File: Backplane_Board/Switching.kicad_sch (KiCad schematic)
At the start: 60 parts, among them J37 Conn_01x02, J38 Conn_01x02, J39 Conn_01x02, J40 Conn_01x02, J41 Conn_01x02, J42 Conn_01x02, Q4 ZXMN3A14F, Q5 ZXMN3A14F, Q6 ZXMN3A14F, Q7 ZXMN3A14F, Q8 ZXMN3A14F, Q9 ZXMN3A14F

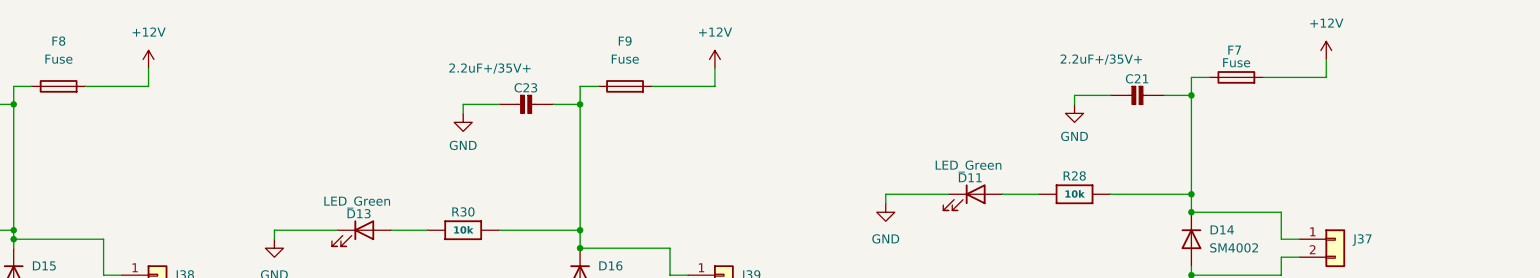
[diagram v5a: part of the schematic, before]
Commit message: got the power input shut layout done ish
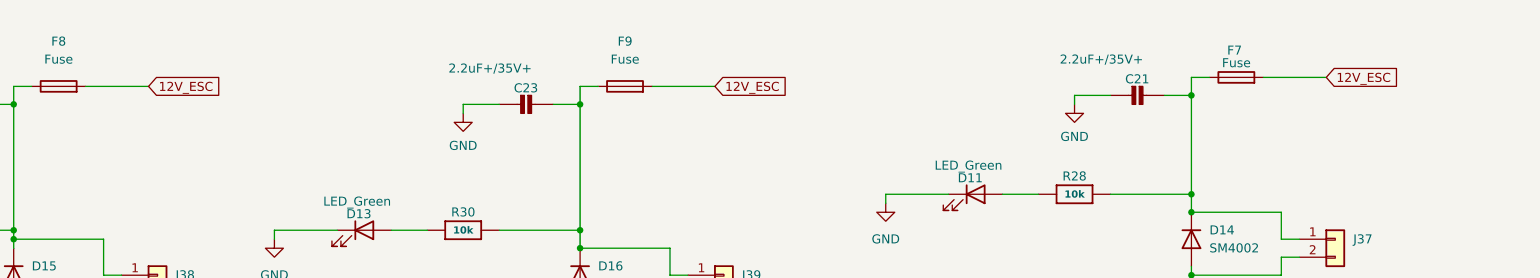
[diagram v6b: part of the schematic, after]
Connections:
- net +12V renamed 12V_ESC
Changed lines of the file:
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@@
 	(wire
 		(pts
-			(xy 162.56 20.32) (xy 162.56 22.86)
-		)
-		(stroke
-			(width 0)
-			(type default)
-		)
-	)
-	(wire
-		(pts
 			(xy 35.56 90.17) (xy 35.56 87.63)
 		)
@@
 	(wire
 		(pts
-			(xy 82.55 20.32) (xy 82.55 22.86)
-		)
-		(stroke
-			(width 0)
-			(type default)
-		)
-	)
-	(wire
-		(pts
 			(xy 143.51 54.61) (xy 156.21 54.61)
 		)
@@
 	(wire
 		(pts
-			(xy 248.92 19.05) (xy 248.92 21.59)
-		)
-		(stroke
-			(width 0)
-			(type default)
-		)
-	)
-	(wire
-		(pts
 			(xy 72.39 140.97) (xy 72.39 144.78)
 		)
@@
 		)
 	)
+	(global_label "12V_ESC"
+		(shape input)
+		(at 248.92 21.59 0)
+		(fields_autoplaced yes)
+		(effects
+			(font
+				(size 1.27 1.27)
+			)
+			(justify left)
+		)
+		(property "Intersheetrefs" "${INTERSHEET_REFS}"
+			(at 260.0089 21.59 0)
+			(effects
+				(font
+					(size 1.27 1.27)
+				)
+				(justify left)
+				(hide yes)
+			)
+		)
+	)
 	(global_label "SW5"
 		(shape input)
@@
 		)
 	)
+	(global_label "12V_ESC"
+		(shape input)
+		(at 162.56 22.86 0)
+		(fields_autoplaced yes)
+		(effects
+			(font
+				(size 1.27 1.27)
+			)
+			(justify left)
+		)
+		(property "Intersheetrefs" "${INTERSHEET_REFS}"
+			(at 173.6489 22.86 0)
+			(effects
+				(font
+					(size 1.27 1.27)
+				)
+				(justify left)
+				(hide yes)
+			)
+		)
+	)
+	(global_label "12V_ESC"
+		(shape input)
+		(at 82.55 22.86 0)
+		(fields_autoplaced yes)
+		(effects
+			(font
+				(size 1.27 1.27)
+			)
+			(justify left)
+		)
+		(property "Intersheetrefs" "${INTERSHEET_REFS}"
+			(at 93.6389 22.86 0)
+			(effects
+				(font
+					(size 1.27 1.27)
+				)
+				(justify left)
+				(hide yes)
+			)
+		)
+	)
 	(global_label "SW0"
 		(shape input)
@@
 	)
 	(symbol
-		(lib_id "power:+12V")
-		(at 82.55 20.32 0)
-		(unit 1)
-		(exclude_from_sim no)
-		(in_bom yes)
-		(on_board yes)
-		(dnp no)
-		(fields_autoplaced yes)
-		(property "Reference" "#PWR083"
-			(at 82.55 24.13 0)
-			(effects
-				(font
-					(size 1.27 1.27)
-				)
-				(hide yes)
-			)
-		)
-		(property "Value" "+12V"
-			(at 82.55 15.24 0)
-			(effects
-				(font
-					(size 1.27 1.27)
-				)
-			)
-		)
-		(property "Footprint" ""
-			(at 82.55 20.32 0)
-			(effects
-				(font
-					(size 1.27 1.27)
-				)
-				(hide yes)
-			)
-		)
-		(property "Datasheet" ""
-			(at 82.55 20.32 0)
-			(effects
-				(font
-					(size 1.27 1.27)
-				)
-				(hide yes)
-			)
-		)
-		(property "Description" "Power symbol creates a global label with name \"+12V\""
-			(at 82.55 20.32 0)
-			(effects
-				(font
-					(size 1.27 1.27)
-				)
-				(hide yes)
-			)
-		)
-		(pin "1"
-		)
-		(instances
-			(project "Backplane_Board"
-				(path "/4484cfee-9e43-4cef-88b4-a8ca308542b4/31bf6b29-9be4-43f9-9eab-c84ca2b3429e"
-					(reference "#PWR083")
-					(unit 1)
-				)
-			)
-		)
-	)
-	(symbol
 		(lib_id "power:GND")
 		(at 143.51 69.85 0)
@@
 	)
 	(symbol
-		(lib_id "power:+12V")
-		(at 248.92 19.05 0)
-		(unit 1)
-		(exclude_from_sim no)
-		(in_bom yes)
-		(on_board yes)
-		(dnp no)
-		(fields_autoplaced yes)
-		(property "Reference" "#PWR082"
-			(at 248.92 22.86 0)
-			(effects
-				(font
-					(size 1.27 1.27)
-				)
-				(hide yes)
-			)
-		)
-		(property "Value" "+12V"
-			(at 248.92 13.97 0)
-			(effects
-				(font
-					(size 1.27 1.27)
-				)
-			)
-		)
-		(property "Footprint" ""
-			(at 248.92 19.05 0)
-			(effects
-				(font
-					(size 1.27 1.27)
-				)
-				(hide yes)
-			)
-		)
-		(property "Datasheet" ""
-			(at 248.92 19.05 0)
-			(effects
-				(font
-					(size 1.27 1.27)
-				)
-				(hide yes)
-			)
-		)
-		(property "Description" "Power symbol creates a global label with name \"+12V\""
-			(at 248.92 19.05 0)
-			(effects
-				(font
-					(size 1.27 1.27)
-				)
-				(hide yes)
-			)
-		)
-		(pin "1"
-		)
-		(instances
-			(project "Backplane_Board"
-				(path "/4484cfee-9e43-4cef-88b4-a8ca308542b4/31bf6b29-9be4-43f9-9eab-c84ca2b3429e"
-					(reference "#PWR082")
-					(unit 1)
-				)
-			)
-		)
-	)
-	(symbol
 		(lib_id "Adafruit MOSFET Driver STEMMA Breakout-eagle-import:CAP_CERAMIC0805-NOOUTLINE")
 		(at 140.97 125.73 270)
@@
 					(unit 1)
 				)
-			)
-		)
-	)
-	(symbol
-		(lib_id "power:+12V")
-		(at 162.56 20.32 0)
-		(unit 1)
-		(exclude_from_sim no)
-		(in_bom yes)
-		(on_board yes)
-		(dnp no)
-		(fields_autoplaced yes)
-		(property "Reference" "#PWR084"
-			(at 162.56 24.13 0)
-			(effects
-				(font
-					(size 1.27 1.27)
-				)
-				(hide yes)
-			)
-		)
-		(property "Value" "+12V"
-			(at 162.56 15.24 0)
-			(effects
-				(font
-					(size 1.27 1.27)
-				)
-			)
-		)
-		(property "Footprint" ""
-			(at 162.56 20.32 0)
-			(effects
-				(font
-					(size 1.27 1.27)
-				)
-				(hide yes)
-			)
-		)
-		(property "Datasheet" ""
-			(at 162.56 20.32 0)
-			(effects
-				(font
-					(size 1.27 1.27)
-				)
-				(hide yes)
-			)
-		)
-		(property "Description" "Power symbol creates a global label with name \"+12V\""
-			(at 162.56 20.32 0)
-			(effects
-				(font
-					(size 1.27 1.27)
-				)
-				(hide yes)
-			)
-		)
-		(pin "1"
-		)
-		(instances
-			(project "Backplane_Board"
-				(path "/4484cfee-9e43-4cef-88b4-a8ca308542b4/31bf6b29-9be4-43f9-9eab-c84ca2b3429e"
-					(reference "#PWR084")
-					(unit 1)
-				)

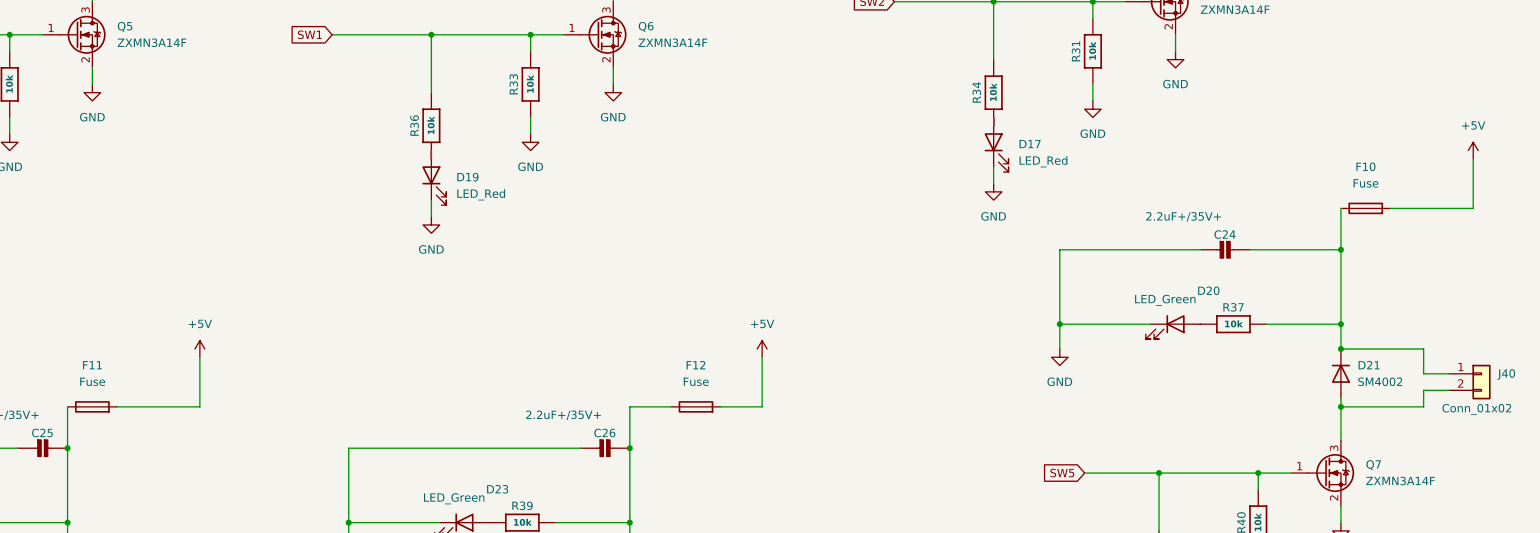
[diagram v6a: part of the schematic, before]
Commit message: rough layout compleat, 200+ drc errors to fix
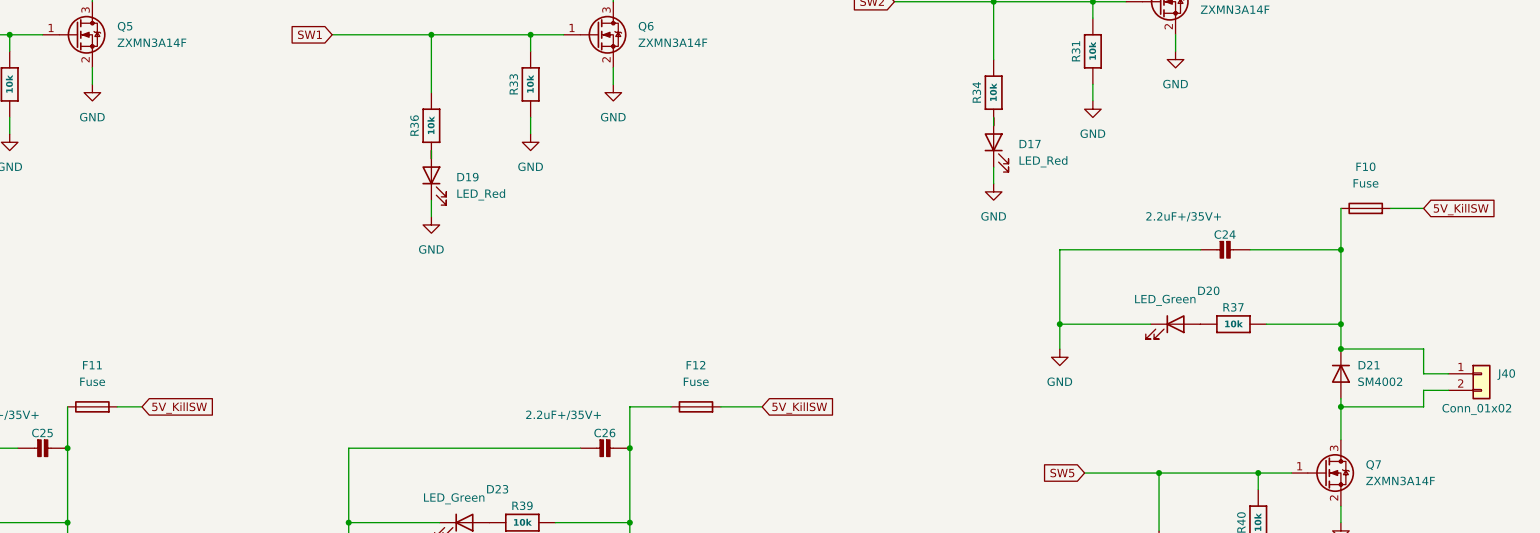
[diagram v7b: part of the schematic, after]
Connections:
- net +5V renamed 5V_KillSW
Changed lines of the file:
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@@
 	(wire
 		(pts
-			(xy 67.31 119.38) (xy 80.01 119.38)
+			(xy 67.31 119.38) (xy 71.12 119.38)
 		)
 		(stroke
@@
 	(wire
 		(pts
-			(xy 80.01 111.76) (xy 80.01 119.38)
-		)
-		(stroke
-			(width 0)
-			(type default)
-		)
-	)
-	(wire
-		(pts
 			(xy 227.33 129.54) (xy 242.57 129.54)
 		)
@@
 	(wire
 		(pts
-			(xy 262.89 88.9) (xy 275.59 88.9)
+			(xy 262.89 88.9) (xy 267.97 88.9)
 		)
 		(stroke
@@
 	(wire
 		(pts
-			(xy 275.59 81.28) (xy 275.59 88.9)
-		)
-		(stroke
-			(width 0)
-			(type default)
-		)
-	)
-	(wire
-		(pts
 			(xy 143.51 54.61) (xy 143.51 57.15)
 		)
@@
 	(wire
 		(pts
-			(xy 166.37 111.76) (xy 166.37 119.38)
-		)
-		(stroke
-			(width 0)
-			(type default)
-		)
-	)
-	(wire
-		(pts
 			(xy 243.84 106.68) (xy 255.27 106.68)
 		)
@@
 		)
 	)
+	(global_label "5V_KillSW"
+		(shape input)
+		(at 71.12 119.38 0)
+		(fields_autoplaced yes)
+		(effects
+			(font
+				(size 1.27 1.27)
+			)
+			(justify left)
+		)
+		(property "Intersheetrefs" "${INTERSHEET_REFS}"
+			(at 83.237 119.38 0)
+			(effects
+				(font
+					(size 1.27 1.27)
+				)
+				(justify left)
+				(hide yes)
+			)
+		)
+	)
 	(global_label "12V_ESC"
 		(shape input)
@@
 		)
 	)
+	(global_label "5V_KillSW"
+		(shape input)
+		(at 267.97 88.9 0)
+		(fields_autoplaced yes)
+		(effects
+			(font
+				(size 1.27 1.27)
+			)
+			(justify left)
+		)
+		(property "Intersheetrefs" "${INTERSHEET_REFS}"
+			(at 280.087 88.9 0)
+			(effects
+				(font
+					(size 1.27 1.27)
+				)
+				(justify left)
+				(hide yes)
+			)
+		)
+	)
+	(global_label "5V_KillSW"
+		(shape input)
+		(at 166.37 119.38 0)
+		(fields_autoplaced yes)
+		(effects
+			(font
+				(size 1.27 1.27)
+			)
+			(justify left)
+		)
+		(property "Intersheetrefs" "${INTERSHEET_REFS}"
+			(at 178.487 119.38 0)
+			(effects
+				(font
+					(size 1.27 1.27)
+				)
+				(justify left)
+				(hide yes)
+			)
+		)
+	)
 	(global_label "12V_ESC"
 		(shape input)
@@
 	)
 	(symbol
-		(lib_id "power:+5V")
-		(at 166.37 111.76 0)
-		(unit 1)
-		(exclude_from_sim no)
-		(in_bom yes)
-		(on_board yes)
-		(dnp no)
-		(fields_autoplaced yes)
-		(property "Reference" "#PWR0103"
-			(at 166.37 115.57 0)
-			(effects
-				(font
-					(size 1.27 1.27)
-				)
-				(hide yes)
-			)
-		)
-		(property "Value" "+5V"
-			(at 166.37 106.68 0)
-			(effects
-				(font
-					(size 1.27 1.27)
-				)
-			)
-		)
-		(property "Footprint" ""
-			(at 166.37 111.76 0)
-			(effects
-				(font
-					(size 1.27 1.27)
-				)
-				(hide yes)
-			)
-		)
-		(property "Datasheet" ""
-			(at 166.37 111.76 0)
-			(effects
-				(font
-					(size 1.27 1.27)
-				)
-				(hide yes)
-			)
-		)
-		(property "Description" "Power symbol creates a global label with name \"+5V\""
-			(at 166.37 111.76 0)
-			(effects
-				(font
-					(size 1.27 1.27)
-				)
-				(hide yes)
-			)
-		)
-		(pin "1"
-		)
-		(instances
-			(project "Backplane_Board"
-				(path "/4484cfee-9e43-4cef-88b4-a8ca308542b4/31bf6b29-9be4-43f9-9eab-c84ca2b3429e"
-					(reference "#PWR0103")
-					(unit 1)
-				)
-			)
-		)
-	)
-	(symbol
 		(lib_id "power:GND")
 		(at 59.69 167.64 0)
@@
 	)
 	(symbol
-		(lib_id "power:+5V")
-		(at 275.59 81.28 0)
-		(unit 1)
-		(exclude_from_sim no)
-		(in_bom yes)
-		(on_board yes)
-		(dnp no)
-		(fields_autoplaced yes)
-		(property "Reference" "#PWR097"
-			(at 275.59 85.09 0)
-			(effects
-				(font
-					(size 1.27 1.27)
-				)
-				(hide yes)
-			)
-		)
-		(property "Value" "+5V"
-			(at 275.59 76.2 0)
-			(effects
-				(font
-					(size 1.27 1.27)
-				)
-			)
-		)
-		(property "Footprint" ""
-			(at 275.59 81.28 0)
-			(effects
-				(font
-					(size 1.27 1.27)
-				)
-				(hide yes)
-			)
-		)
-		(property "Datasheet" ""
-			(at 275.59 81.28 0)
-			(effects
-				(font
-					(size 1.27 1.27)
-				)
-				(hide yes)
-			)
-		)
-		(property "Description" "Power symbol creates a global label with name \"+5V\""
-			(at 275.59 81.28 0)
-			(effects
-				(font
-					(size 1.27 1.27)
-				)
-				(hide yes)
-			)
-		)
-		(pin "1"
-		)
-		(instances
-			(project "Backplane_Board"
-				(path "/4484cfee-9e43-4cef-88b4-a8ca308542b4/31bf6b29-9be4-43f9-9eab-c84ca2b3429e"
-					(reference "#PWR097")
-					(unit 1)
-				)
-			)
-		)
-	)
-	(symbol
 		(lib_id "Transistor_FET:ZXMN3A14F")
 		(at 140.97 62.23 0)
@@
 					(unit 1)
 				)
-			)
-		)
-	)
-	(symbol
-		(lib_id "power:+5V")
-		(at 80.01 111.76 0)
-		(unit 1)
-		(exclude_from_sim no)
-		(in_bom yes)
-		(on_board yes)
-		(dnp no)
-		(fields_autoplaced yes)
-		(property "Reference" "#PWR0102"
-			(at 80.01 115.57 0)
-			(effects
-				(font
-					(size 1.27 1.27)
-				)
-				(hide yes)
-			)
-		)
-		(property "Value" "+5V"
-			(at 80.01 106.68 0)
-			(effects
-				(font
-					(size 1.27 1.27)
-				)
-			)
-		)
-		(property "Footprint" ""
-			(at 80.01 111.76 0)
-			(effects
-				(font
-					(size 1.27 1.27)
-				)
-				(hide yes)
-			)
-		)
-		(property "Datasheet" ""
-			(at 80.01 111.76 0)
-			(effects
-				(font
-					(size 1.27 1.27)
-				)
-				(hide yes)
-			)
-		)
-		(property "Description" "Power symbol creates a global label with name \"+5V\""
-			(at 80.01 111.76 0)
-			(effects
-				(font
-					(size 1.27 1.27)
-				)
-				(hide yes)
-			)
-		)
-		(pin "1"
-		)
-		(instances
-			(project "Backplane_Board"
-				(path "/4484cfee-9e43-4cef-88b4-a8ca308542b4/31bf6b29-9be4-43f9-9eab-c84ca2b3429e"
-					(reference "#PWR0102")
-					(unit 1)
-				)

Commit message: added gerber
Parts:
- R34, R35, R36, R41, R44, R45: value 10k -> 2k
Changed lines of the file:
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@@
 			)
 		)
-		(property "Value" "10k"
+		(property "Value" "2k"
 			(at 115.57 76.2 0)
 			(effects
@@
 			)
 		)
-		(property "Value" "10k"
+		(property "Value" "2k"
 			(at 227.33 143.51 0)
 			(effects
@@
 			)
 		)
-		(property "Value" "10k"
+		(property "Value" "2k"
 			(at 118.11 173.99 0)
 			(effects
@@
 			)
 		)
-		(property "Value" "10k"
+		(property "Value" "2k"
 			(at 35.56 76.2 0)
 			(effects
@@
 			)
 		)
-		(property "Value" "10k"
+		(property "Value" "2k"
 			(at 201.93 71.12 0)
 			(effects
@@
 			)
 		)
-		(property "Value" "10k"
+		(property "Value" "2k"
 			(at 31.75 173.99 0)
 			(effects
